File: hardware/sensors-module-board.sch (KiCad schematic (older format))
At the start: 14 parts, among them IC1 SHTC3, J1 I2C_HEADER, U1 SGPC3-2.5k, U2 PCA9306

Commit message: Added BOM printout and started PCB import
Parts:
- C1, C2, C3, C4, C5, C6: footprint (none) -> Capacitors_SMD:C_1206
- IC1: footprint SHTC3 -> SHTC3:SHTC3
- J1: footprint (none) -> Pin_Headers:Pin_Header_Straight_1x04_Pitch2.54mm
- PS1: footprint SOT95P280X145-5N -> TPS78918DBVT:SOT95P280X145-5N
- R1, R2, R3: footprint (none) -> Resistors_SMD:R_1206
- U1: footprint SON80P245X245X90-7N -> SGPC3-2.5k:SON80P245X245X90-7N
- U2: footprint (none) -> PCA9306TDCURQ1:SOP50P310X90-8N
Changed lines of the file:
@@
 F 0 "U2" H 5050 4650 50  0000 L CNN
 F 1 "PCA9306" H 5550 4650 50  0000 L CNN
-F 2 "" H 4950 4550 50  0001 C CNN
+F 2 "PCA9306TDCURQ1:SOP50P310X90-8N" H 4950 4550 50  0001 C CNN
 F 3 "" H 5050 4650 50  0001 C CNN
 	1    5350 4200
@@
 F 0 "R1" H 6180 3570 50  0000 L CNN
 F 1 "200k" H 6180 3510 50  0000 L CNN
-F 2 "" H 6150 3550 50  0001 C CNN
+F 2 "Resistors_SMD:R_1206" H 6150 3550 50  0001 C CNN
 F 3 "" H 6150 3550 50  0001 C CNN
 	1    6150 3550
@@
 F 0 "C2" H 6160 3970 50  0000 L CNN
 F 1 "100pF" H 6160 3820 50  0000 L CNN
-F 2 "" H 6150 3900 50  0001 C CNN
+F 2 "Capacitors_SMD:C_1206" H 6150 3900 50  0001 C CNN
 F 3 "" H 6150 3900 50  0001 C CNN
 	1    6150 3900
@@
 F 0 "R3" H 4830 3970 50  0000 L CNN
 F 1 "200k" H 4830 3910 50  0000 L CNN
-F 2 "" H 4800 3950 50  0001 C CNN
+F 2 "Resistors_SMD:R_1206" H 4800 3950 50  0001 C CNN
 F 3 "" H 4800 3950 50  0001 C CNN
 	1    4800 3950
@@
 F 0 "R2" H 4530 3970 50  0000 L CNN
 F 1 "200k" H 4530 3910 50  0000 L CNN
-F 2 "" H 4500 3950 50  0001 C CNN
+F 2 "Resistors_SMD:R_1206" H 4500 3950 50  0001 C CNN
 F 3 "" H 4500 3950 50  0001 C CNN
 	1    4500 3950
@@
 F 0 "C3" H 2260 4220 50  0000 L CNN
 F 1 "100nF" H 2260 4070 50  0000 L CNN
-F 2 "" H 2250 4150 50  0001 C CNN
+F 2 "Capacitors_SMD:C_1206" H 2250 4150 50  0001 C CNN
 F 3 "" H 2250 4150 50  0001 C CNN
 	1    2250 4150
@@
 F 0 "C1" H 7910 3020 50  0000 L CNN
 F 1 "100nF" H 7910 2870 50  0000 L CNN
-F 2 "" H 7900 2950 50  0001 C CNN
+F 2 "Capacitors_SMD:C_1206" H 7900 2950 50  0001 C CNN
 F 3 "" H 7900 2950 50  0001 C CNN
 	1    7900 2950
@@
 F 0 "IC1" H 7850 3100 50  0000 L CNN
 F 1 "SHTC3" H 7900 2950 50  0000 L CNN
-F 2 "SHTC3" H 8250 3250 50  0001 L CNN
+F 2 "SHTC3:SHTC3" H 8250 3250 50  0001 L CNN
 F 3 "https://www.glynshop.com/erp/owweb/Daten/Datenblaetter/Sensirion/SHTC3.pdf" H 8250 3150 50  0001 L CNN
 F 4 "Humidity and Temperature Sensor IC" H 8250 3050 50  0001 L CNN "Description"
@@
 F 0 "U1" H 3450 3700 50  0000 L CNN
 F 1 "SGPC3-2.5k" H 3000 3850 50  0000 L CNN
-F 2 "SON80P245X245X90-7N" H 3650 4300 50  0001 L CNN
+F 2 "SGPC3-2.5k:SON80P245X245X90-7N" H 3650 4300 50  0001 L CNN
 F 3 "https://componentsearchengine.com/Datasheets/2/SGPC3-2.5K.pdf" H 3650 4200 50  0001 L CNN
 F 4 "SENSIRION - SGPC3-2.5K - DIGITAL LOW POWER GAS SENSOR, 1.8V, DFN" H 3650 4100 50  0001 L CNN "Description"
@@
 F 0 "PS1" H 2850 6200 50  0000 L CNN
 F 1 "TPS78918DBVR" H 2750 6050 50  0000 L CNN
-F 2 "SOT95P280X145-5N" H 2400 5700 50  0001 L CNN
+F 2 "TPS78918DBVT:SOT95P280X145-5N" H 2400 5700 50  0001 L CNN
 F 3 "http://www.ti.com/lit/ds/symlink/tps789.pdf" H 2400 5550 50  0001 L CNN
 F 4 "Texas Instruments TPS78918DBVR, LDO Voltage Regulator, 0.1A, 1.8 V, 2.7  10 Vin, 5-Pin SOT-23" H 2400 5400 50  0001 L CNN "Description"
@@
 F 0 "C6" H 1910 6670 50  0000 L CNN
 F 1 "1uF" H 1910 6520 50  0000 L CNN
-F 2 "" H 1900 6600 50  0001 C CNN
+F 2 "Capacitors_SMD:C_1206" H 1900 6600 50  0001 C CNN
 F 3 "" H 1900 6600 50  0001 C CNN
 	1    1900 6600
@@
 F 0 "C5" H 3710 6620 50  0000 L CNN
 F 1 "4.7uF (0.2-10 Ohm ESR)" H 3710 6470 50  0000 L CNN
-F 2 "" H 3700 6550 50  0001 C CNN
+F 2 "Capacitors_SMD:C_1206" H 3700 6550 50  0001 C CNN
 F 3 "" H 3700 6550 50  0001 C CNN
 	1    3700 6550
@@
 F 0 "C4" H 4760 6570 50  0000 L CNN
 F 1 "0.01uF" H 4760 6420 50  0000 L CNN
-F 2 "" H 4750 6500 50  0001 C CNN
+F 2 "Capacitors_SMD:C_1206" H 4750 6500 50  0001 C CNN
 F 3 "" H 4750 6500 50  0001 C CNN
 	1    4750 6500
@@
 F 0 "J1" H 9700 4300 50  0000 C CNN
 F 1 "I2C_HEADER" H 9700 3800 50  0000 C CNN
-F 2 "" H 9700 4100 50  0001 C CNN
+F 2 "Pin_Headers:Pin_Header_Straight_1x04_Pitch2.54mm" H 9700 4100 50  0001 C CNN
 F 3 "" H 9700 4100 50  0001 C CNN
 	1    9700 4100

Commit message: Added first PCB draft
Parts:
- added J2: I2C_boardconnector, badgeComponents:I2C_header_halfround_Pitch2.54mm, symbol I2C_HEADER
- added J3: BOARD_CONNECTOR, badgeComponents:GND_BOARD_CONNECTOR_halfround_Pitch2.54mm, symbol BOARD_CONNECTOR
- J1: footprint Pin_Headers:Pin_Header_Straight_1x04_Pitch2.54mm -> badgeComponents:I2C_header_Pitch2.54mm
- renumbered IC1 to U3
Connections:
- net +3V3: now also J2.VCC
- net GND: now also J2.GND, J3.GND
- net at J1.SDA, U2.5 (SDA2), U3.3 (SDA): now also J2.SDA
- net at J1.SCL, U2.6 (SCL2), U3.2 (SCL): now also J2.SCL

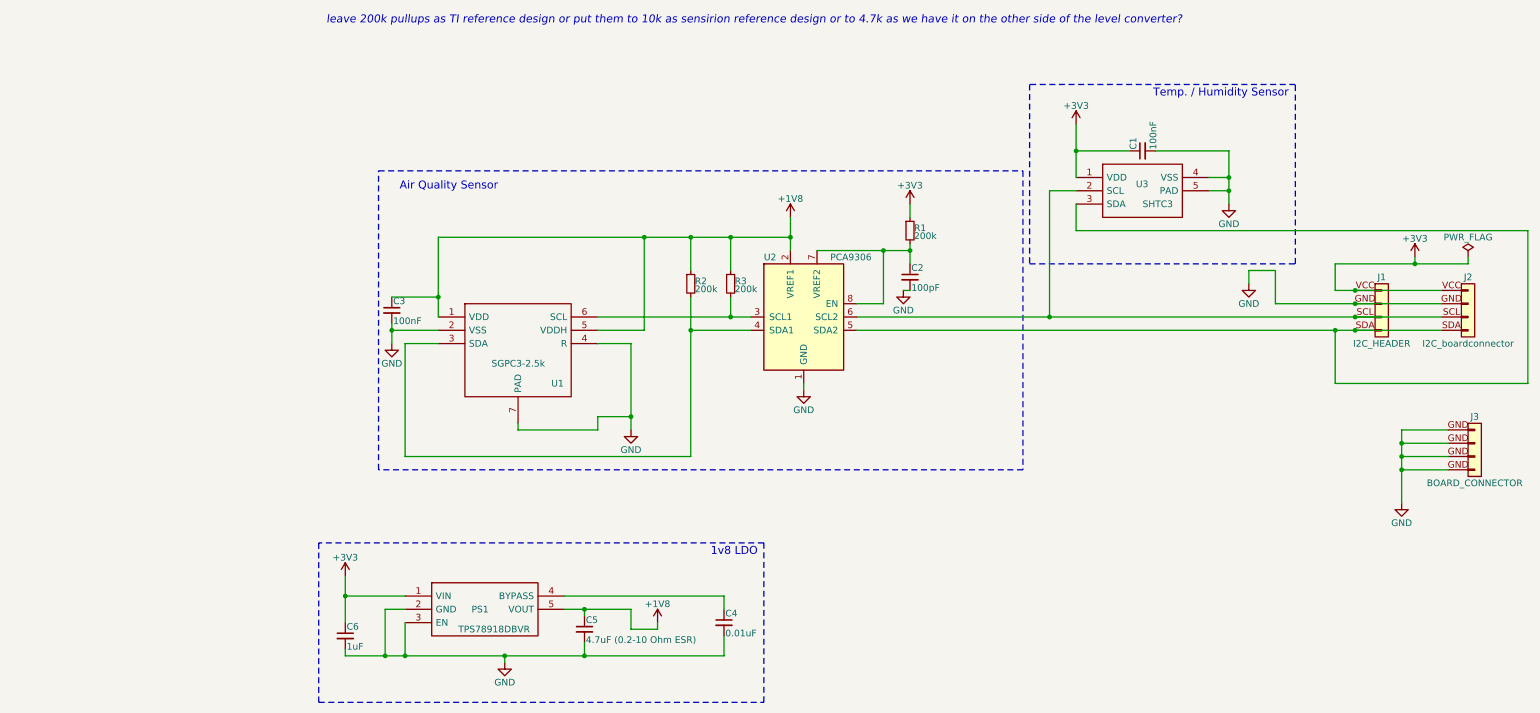
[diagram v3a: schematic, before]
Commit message: Added files for pick and place
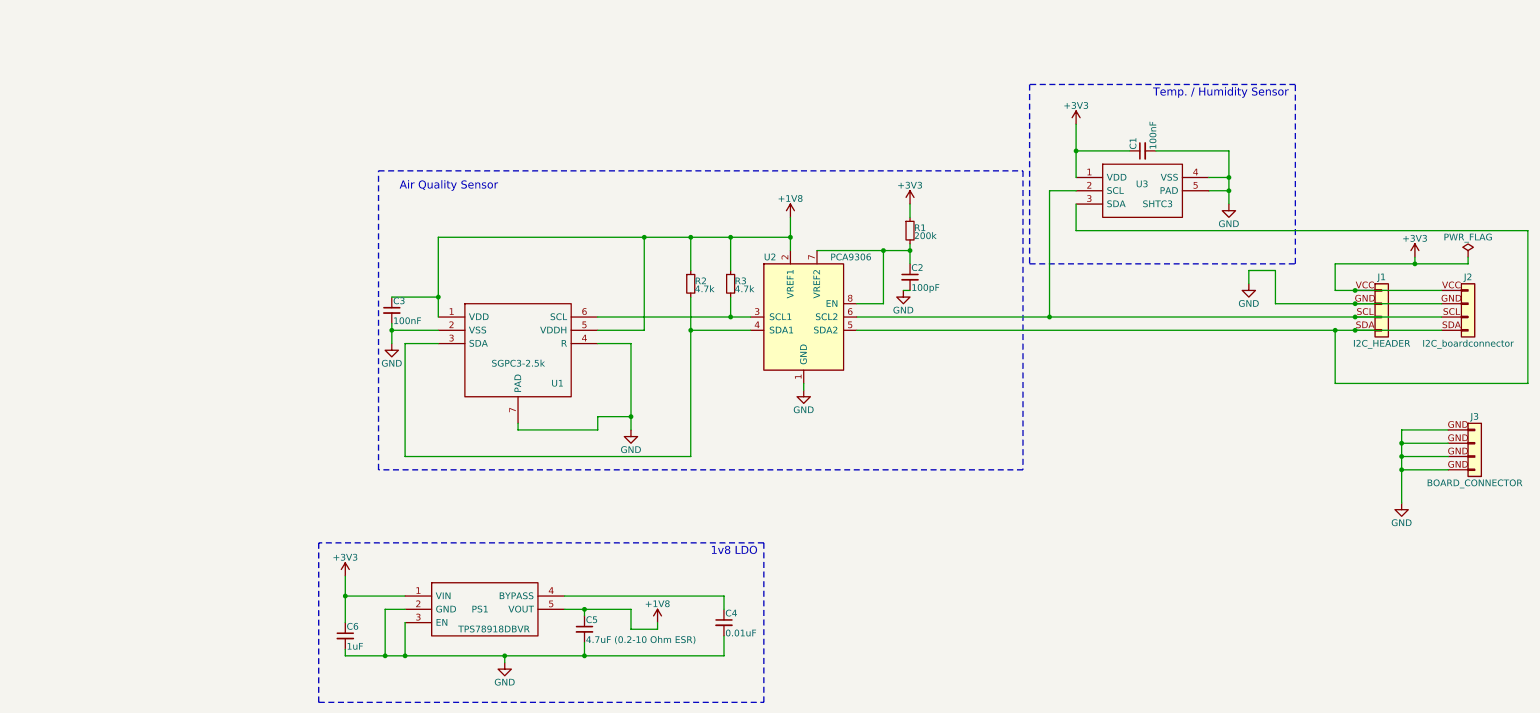
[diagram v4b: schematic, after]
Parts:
- R2, R3: value 200k -> 4.7k
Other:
- note removed: "leave 200k pullups as TI reference design or put them to 10k as sensirion reference design or to 4.7k as we have it on the other side of the level converter?"
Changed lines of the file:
@@
 Sheet 1 1
 Title "IoT conference badge - sensors module board"
-Date "2018-05-16"
-Rev "0.1.3"
+Date "2018-06-21"
+Rev "0.1.4"
 Comp "MakeZürich (makezurich.ch) & GDG Zürich (gdgzh.ch)"
 Comment1 ""
@@
 P 4800 3950
 F 0 "R3" H 4830 3970 50  0000 L CNN
-F 1 "200k" H 4830 3910 50  0000 L CNN
+F 1 "4.7k" H 4830 3910 50  0000 L CNN
 F 2 "Resistors_SMD:R_1206" H 4800 3950 50  0001 C CNN
 F 3 "" H 4800 3950 50  0001 C CNN
@@
 P 4500 3950
 F 0 "R2" H 4530 3970 50  0000 L CNN
-F 1 "200k" H 4530 3910 50  0000 L CNN
+F 1 "4.7k" H 4530 3910 50  0000 L CNN
 F 2 "Resistors_SMD:R_1206" H 4500 3950 50  0001 C CNN
 F 3 "" H 4500 3950 50  0001 C CNN
@@
 	1    0    0    -1
 $EndComp
-Text Notes 8200 2000 2    60   Italic 0
-leave 200k pullups as TI reference design or put them to 10k as sensirion reference design or to 4.7k as we have it on the other side of the level converter?
 $Comp
 L GND #PWR08
